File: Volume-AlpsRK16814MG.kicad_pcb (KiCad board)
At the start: 2 copper layers, 62.2 x 32.4 mm, 7 parts, among them P1 AB I/O, P2 CD I/O, P3 VD, P4 CTRL, U1 SN754410

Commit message: Routed.
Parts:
- moved C1 0.51 mm to (121.2, 110.5)
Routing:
- net +5VD: track 0.00 -> 57.6 mm
- net GND: track 16.5 -> 68.7 mm, vias 0 -> 4
- net DGND: track 7.89 -> 52.4 mm
- net /VOL_UP: track 0.00 -> 31.3 mm
- net /C_TOP: track 0.00 -> 29.9 mm
- net /A_TOP: track 0.00 -> 25.8 mm
- net /D_TOP: track 0.00 -> 24.9 mm
- net /CD_COMMON: track 0.00 -> 24.7 mm
- net /B_TOP: track 0.00 -> 22.9 mm
- net /B_WIPER: track 0.00 -> 22.3 mm
- net /D_WIPER: track 0.00 -> 20.2 mm
- net /AB_COMMON: track 0.00 -> 17.5 mm
- net /C_WIPER: track 0.00 -> 15.9 mm
- net /A_WIPER: track 0.00 -> 12.1 mm
- net /VOL_DOWN: track 0.00 -> 11.7 mm
- added copper zone on B.Cu, net DGND
- added copper zone on F.Cu, net DGND
- added copper zone on F.Cu, net GND
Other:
- board size 62.2 x 32.4 mm -> 62.9 x 32.4 mm

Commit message: Flooded.
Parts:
- added P5: GND, mfk-AVA-20ga, F.Cu at (144.1, 116.2)
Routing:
- net GND: track 68.7 -> 95.9 mm, vias 4 -> 7
- added copper zone on B.Cu, net GND

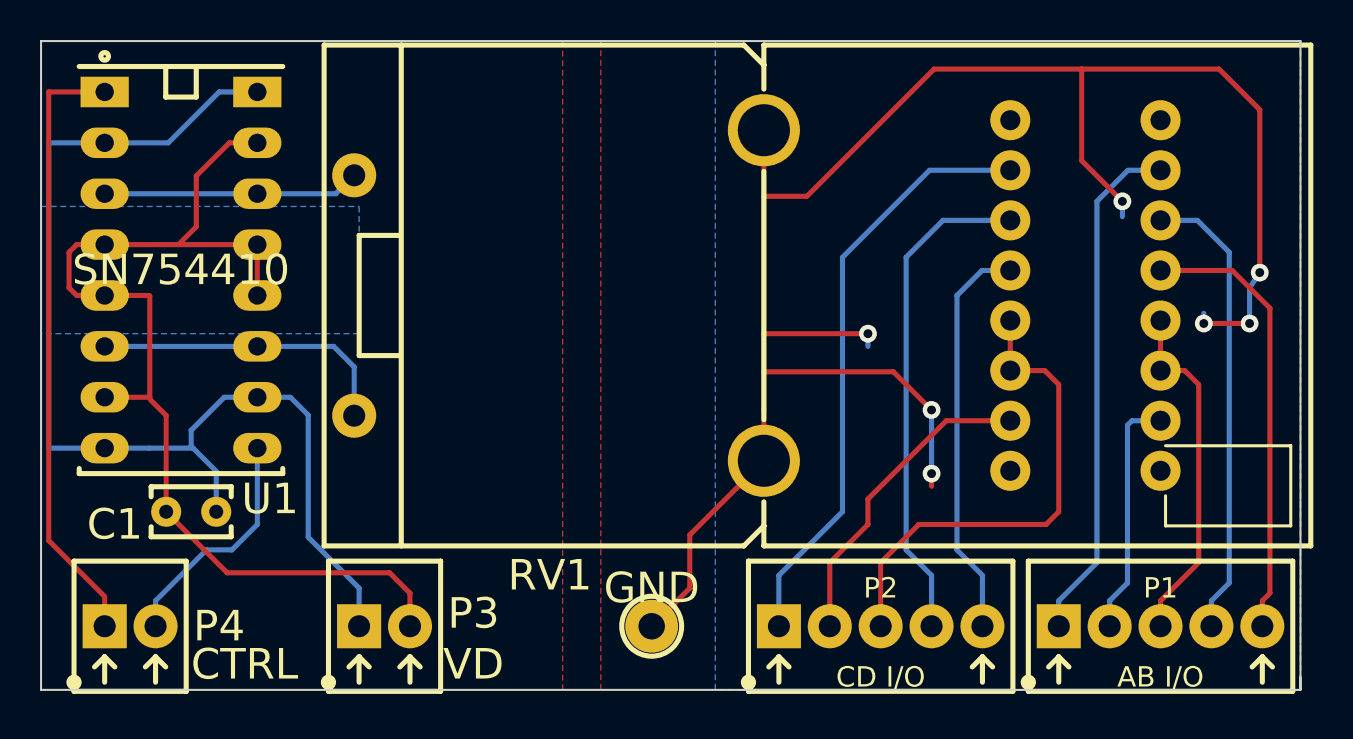
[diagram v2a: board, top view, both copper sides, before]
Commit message: Added bypass C to VCC2.
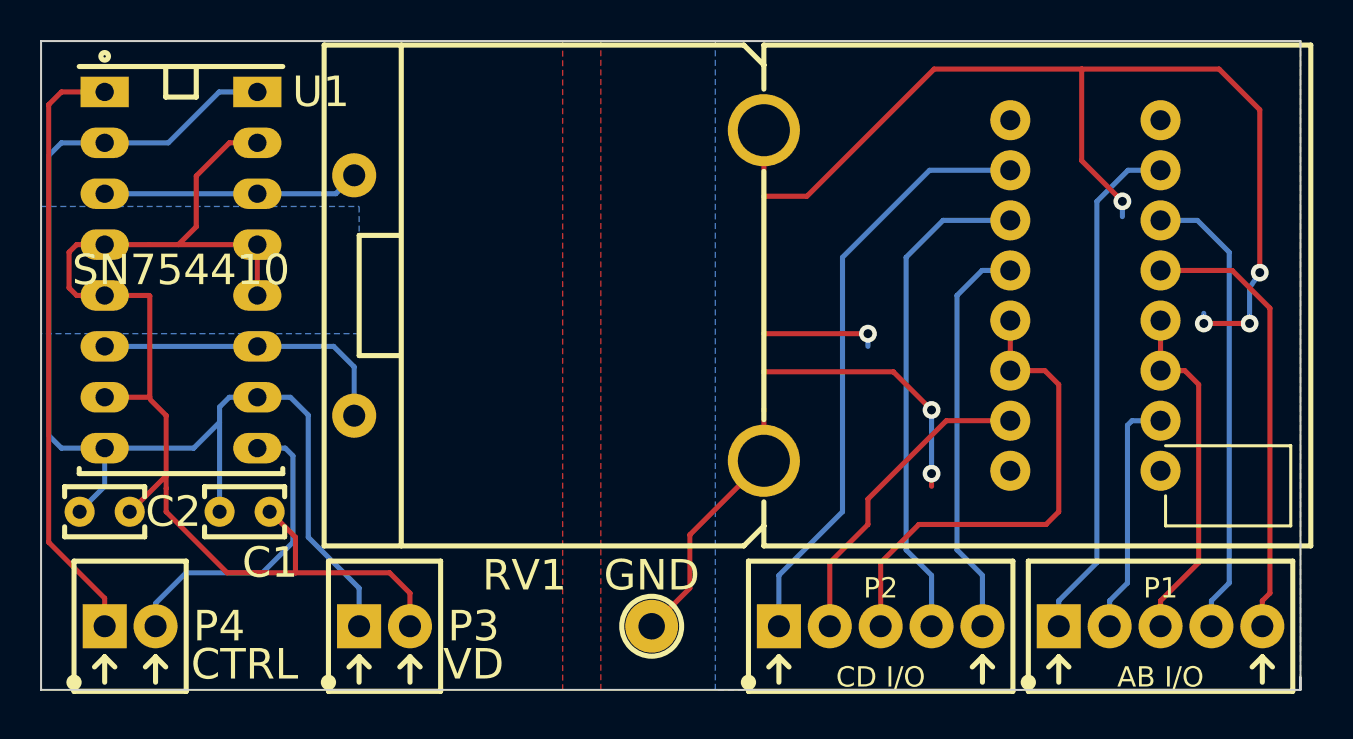
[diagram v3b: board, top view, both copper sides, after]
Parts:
- added C2: 1u, mfk-C_4.0_2.5_2.5_0.5, F.Cu at (116.8, 110.5)
- moved C1 2.67 mm to (123.8, 110.5), turned to 0 degrees
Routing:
- net DGND: track 52.4 -> 58.6 mm
- net /VOL_DOWN: track 11.7 -> 15.5 mm
- net +5VD: track 57.6 -> 60.5 mm
- net /VOL_UP: track 31.3 -> 30.2 mm

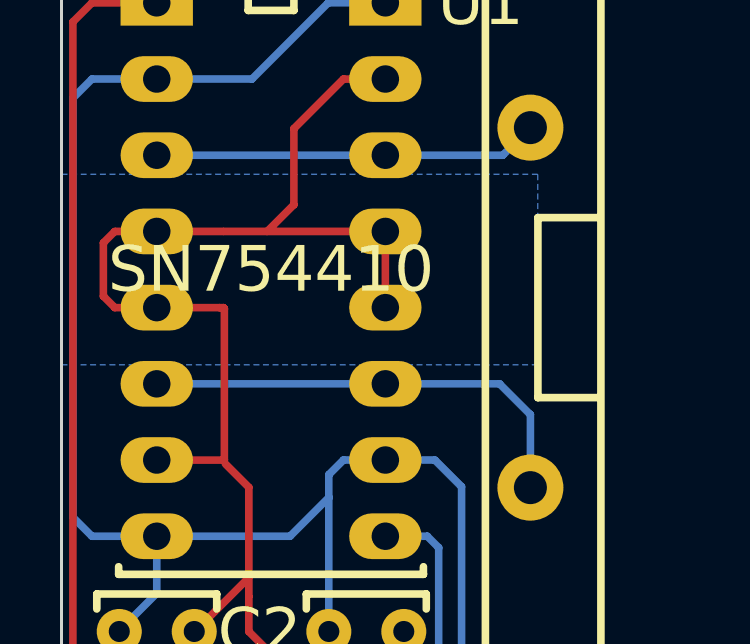
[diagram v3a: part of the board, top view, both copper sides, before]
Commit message: Added cap to VCC2. Stitched SN754410 GND for heat.
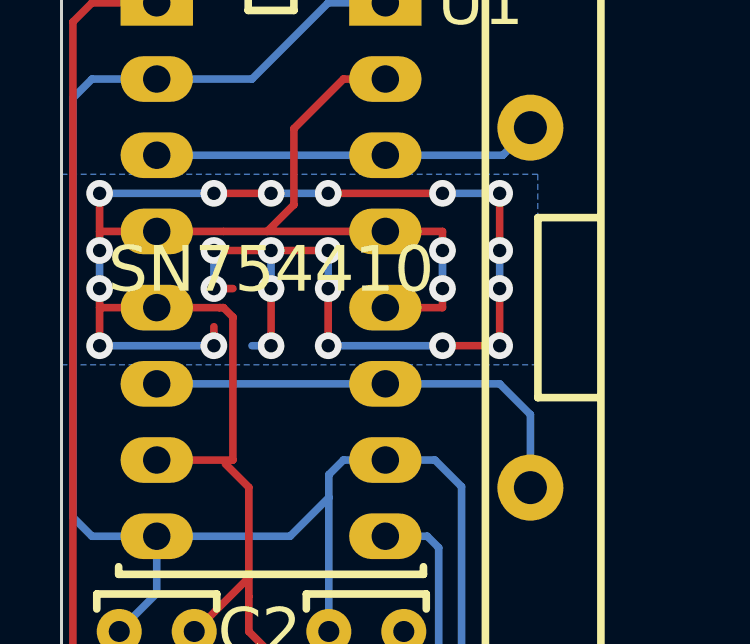
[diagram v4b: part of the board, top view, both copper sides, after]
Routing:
- net DGND: track 58.6 -> 107.3 mm, vias 0 -> 24
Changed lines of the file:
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@@
     (links 34)
     (no_connects 0)
-    (area 113.614999 86.944999 176.580001 119.430001)
+    (area 113.292467 86.559999 187.375714 124.62)
     (thickness 1.6)
     (drawings 7)
-    (tracks 162)
+    (tracks 213)
     (zones 0)
     (modules 9)
@@
   (segment (start 114.046 112.014) (end 114.046 90.17) (width 0.254) (layer F.Cu) (net 13))
   (segment (start 116.84 114.808) (end 114.046 112.014) (width 0.254) (layer F.Cu) (net 13))
+  (segment (start 120.65 97.79) (end 118.745 97.79) (width 0.254) (layer F.Cu) (net 14))
+  (segment (start 118.745 99.06) (end 119.38 99.06) (width 0.254) (layer F.Cu) (net 14))
+  (via (at 118.745 99.06) (size 0.889) (layers F.Cu B.Cu) (net 14))
+  (segment (start 118.745 97.79) (end 118.745 99.06) (width 0.254) (layer B.Cu) (net 14))
+  (via (at 118.745 97.79) (size 0.889) (layers F.Cu B.Cu) (net 14))
+  (segment (start 128.27 100.965) (end 126.365 100.965) (width 0.254) (layer F.Cu) (net 14))
+  (via (at 118.745 95.885) (size 0.889) (layers F.Cu B.Cu) (net 14))
+  (segment (start 118.745 95.885) (end 120.65 95.885) (width 0.254) (layer F.Cu) (net 14))
+  (via (at 120.65 95.885) (size 0.889) (layers F.Cu B.Cu) (net 14))
+  (segment (start 120.65 95.885) (end 122.555 95.885) (width 0.254) (layer B.Cu) (net 14))
+  (via (at 122.555 95.885) (size 0.889) (layers F.Cu B.Cu) (net 14))
+  (segment (start 122.555 95.885) (end 126.365 95.885) (width 0.254) (layer F.Cu) (net 14))
+  (via (at 126.365 95.885) (size 0.889) (layers F.Cu B.Cu) (net 14))
+  (segment (start 126.365 95.885) (end 128.27 95.885) (width 0.254) (layer B.Cu) (net 14))
+  (via (at 128.27 95.885) (size 0.889) (layers F.Cu B.Cu) (net 14))
+  (segment (start 128.27 95.885) (end 128.27 97.79) (width 0.254) (layer F.Cu) (net 14))
+  (via (at 128.27 97.79) (size 0.889) (layers F.Cu B.Cu) (net 14))
+  (segment (start 128.27 97.79) (end 128.27 99.06) (width 0.254) (layer B.Cu) (net 14))
+  (via (at 128.27 99.06) (size 0.889) (layers F.Cu B.Cu) (net 14))
+  (segment (start 128.27 99.06) (end 128.27 100.965) (width 0.254) (layer F.Cu) (net 14))
+  (via (at 128.27 100.965) (size 0.889) (layers F.Cu B.Cu) (net 14))
+  (segment (start 114.935 97.155) (end 114.935 95.885) (width 0.254) (layer F.Cu) (net 14))
+  (via (at 114.935 95.885) (size 0.889) (layers F.Cu B.Cu) (net 14))
+  (segment (start 114.935 95.885) (end 118.745 95.885) (width 0.254) (layer B.Cu) (net 14))
+  (segment (start 120.65 100.965) (end 120.015 100.965) (width 0.254) (layer B.Cu) (net 14))
+  (via (at 120.65 100.965) (size 0.889) (layers F.Cu B.Cu) (net 14))
+  (segment (start 120.65 99.06) (end 120.65 100.965) (width 0.254) (layer F.Cu) (net 14))
+  (via (at 120.65 99.06) (size 0.889) (layers F.Cu B.Cu) (net 14))
+  (segment (start 120.65 97.79) (end 120.65 99.06) (width 0.254) (layer B.Cu) (net 14))
+  (via (at 120.65 97.79) (size 0.889) (layers F.Cu B.Cu) (net 14))
+  (segment (start 122.555 97.79) (end 120.65 97.79) (width 0.254) (layer F.Cu) (net 14))
+  (via (at 122.555 97.79) (size 0.889) (layers F.Cu B.Cu) (net 14))
+  (segment (start 122.555 99.06) (end 122.555 97.79) (width 0.254) (layer B.Cu) (net 14))
+  (via (at 122.555 99.06) (size 0.889) (layers F.Cu B.Cu) (net 14))
+  (segment (start 122.555 100.965) (end 122.555 99.06) (width 0.254) (layer F.Cu) (net 14))
+  (via (at 122.555 100.965) (size 0.889) (layers F.Cu B.Cu) (net 14))
+  (segment (start 126.365 100.965) (end 122.555 100.965) (width 0.254) (layer B.Cu) (net 14))
+  (via (at 126.365 100.965) (size 0.889) (layers F.Cu B.Cu) (net 14))
+  (segment (start 118.745 100.33) (end 118.745 100.965) (width 0.254) (layer F.Cu) (net 14))
+  (via (at 118.745 100.965) (size 0.889) (layers F.Cu B.Cu) (net 14))
+  (segment (start 114.935 100.965) (end 114.935 99.695) (width 0.254) (layer F.Cu) (net 14))
+  (via (at 114.935 100.965) (size 0.889) (layers F.Cu B.Cu) (net 14))
+  (segment (start 114.935 100.965) (end 118.745 100.965) (width 0.254) (layer B.Cu) (net 14))
+  (segment (start 124.46 97.155) (end 126.365 97.155) (width 0.254) (layer F.Cu) (net 14))
+  (segment (start 126.365 99.695) (end 124.46 99.695) (width 0.254) (layer F.Cu) (net 14))
+  (segment (start 126.365 99.06) (end 126.365 99.695) (width 0.254) (layer F.Cu) (net 14))
+  (via (at 126.365 99.06) (size 0.889) (layers F.Cu B.Cu) (net 14))
+  (segment (start 126.365 97.79) (end 126.365 99.06) (width 0.254) (layer B.Cu) (net 14))
+  (via (at 126.365 97.79) (size 0.889) (layers F.Cu B.Cu) (net 14))
+  (segment (start 126.365 97.155) (end 126.365 97.79) (width 0.254) (layer F.Cu) (net 14))
+  (segment (start 116.84 97.155) (end 114.935 97.155) (width 0.254) (layer F.Cu) (net 14))
+  (segment (start 114.935 99.695) (end 116.84 99.695) (width 0.254) (layer F.Cu) (net 14))
+  (segment (start 114.935 99.06) (end 114.935 99.695) (width 0.254) (layer F.Cu) (net 14))
+  (via (at 114.935 99.06) (size 0.889) (layers F.Cu B.Cu) (net 14))
+  (segment (start 114.935 97.79) (end 114.935 99.06) (width 0.254) (layer B.Cu) (net 14))
+  (via (at 114.935 97.79) (size 0.889) (layers F.Cu B.Cu) (net 14))
+  (segment (start 114.935 97.155) (end 114.935 97.79) (width 0.254) (layer F.Cu) (net 14))
   (segment (start 118.08968 110.49) (end 118.11 110.49) (width 0.254) (layer F.Cu) (net 14))
   (segment (start 118.11 110.49) (end 119.90832 108.69168) (width 0.254) (layer F.Cu) (net 14))
@@
   (segment (start 126.365 113.538) (end 122.95632 113.538) (width 0.254) (layer F.Cu) (net 14))
   (segment (start 132.08 114.554) (end 131.064 113.538) (width 0.254) (layer F.Cu) (net 14))
-  (segment (start 116.84 99.695) (end 115.443 99.695) (width 0.254) (layer F.Cu) (net 14))
-  (segment (start 115.443 97.155) (end 116.84 97.155) (width 0.254) (layer F.Cu) (net 14))
-  (segment (start 115.062 97.536) (end 115.443 97.155) (width 0.254) (layer F.Cu) (net 14))
-  (segment (start 115.062 99.314) (end 115.062 97.536) (width 0.254) (layer F.Cu) (net 14))
-  (segment (start 115.443 99.695) (end 115.062 99.314) (width 0.254) (layer F.Cu) (net 14))
   (segment (start 124.46 92.075) (end 123.063 92.075) (width 0.254) (layer F.Cu) (net 14))
   (segment (start 121.412 96.266) (end 120.523 97.155) (width 0.254) (layer F.Cu) (net 14))
@@
   (segment (start 119.0628 97.155) (end 120.523 97.155) (width 0.254) (layer F.Cu) (net 14))
   (segment (start 120.523 97.155) (end 124.46 97.155) (width 0.254) (layer F.Cu) (net 14))
-  (segment (start 124.46 97.155) (end 124.46 99.695) (width 0.254) (layer F.Cu) (net 14))
   (segment (start 132.08 116.205) (end 132.08 114.554) (width 0.254) (layer F.Cu) (net 14))
   (segment (start 117.475 97.155) (end 119.0628 97.155) (width 0.254) (layer F.Cu) (net 14))
-  (segment (start 117.475 104.775) (end 119.0943 104.775) (width 0.254) (layer F.Cu) (net 14))
-  (segment (start 119.0943 99.7265) (end 119.0628 99.695) (width 0.254) (layer F.Cu) (net 14))
-  (segment (start 119.0943 104.775) (end 119.0943 99.7265) (width 0.254) (layer F.Cu) (net 14))
+  (segment (start 117.475 104.775) (end 119.38 104.775) (width 0.254) (layer F.Cu) (net 14))
+  (segment (start 119.38 100.0122) (end 119.0628 99.695) (width 0.254) (layer F.Cu) (net 14))
+  (segment (start 119.38 104.775) (end 119.38 100.0122) (width 0.254) (layer F.Cu) (net 14))
   (segment (start 117.475 99.695) (end 118.9357 99.695) (width 0.254) (layer F.Cu) (net 14))
   (segment (start 118.9357 99.695) (end 119.0628 99.695) (width 0.254) (layer F.Cu) (net 14))

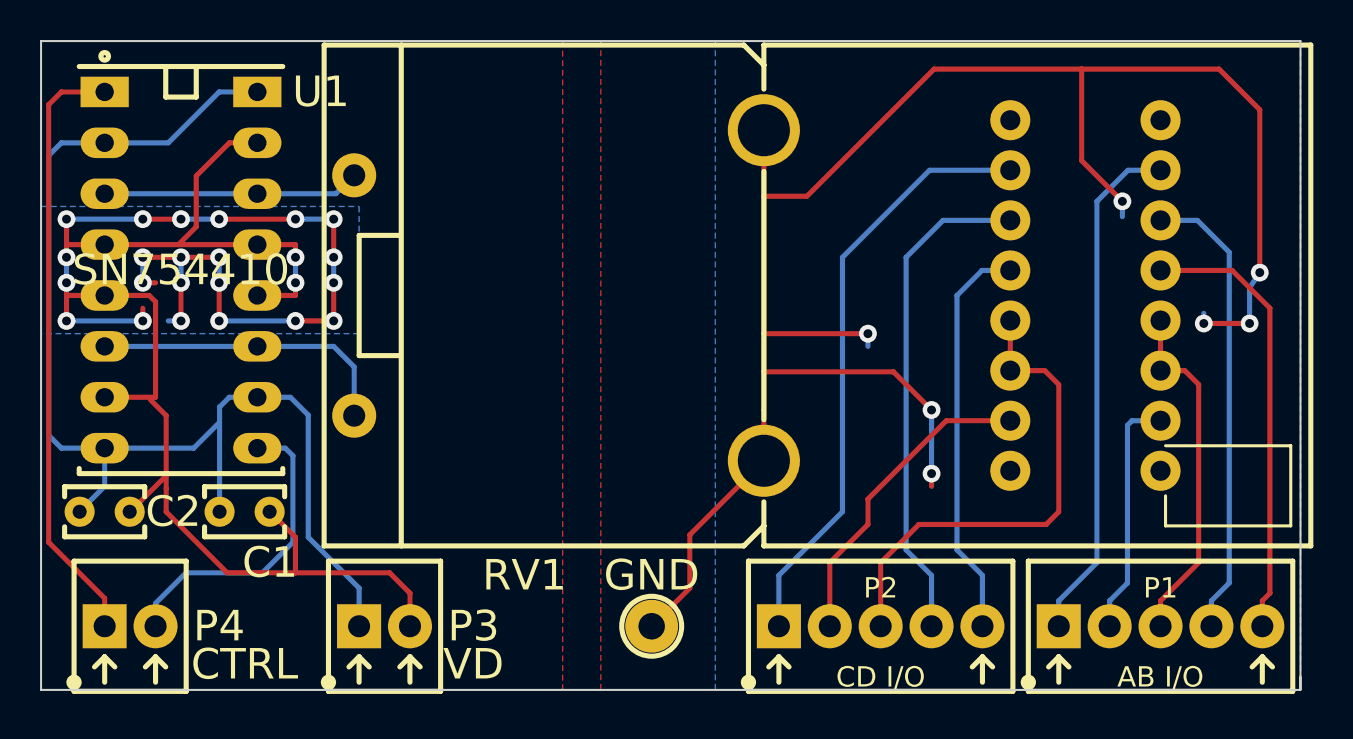
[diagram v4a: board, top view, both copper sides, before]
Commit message: Added (C) and other additional labels silkscreen.
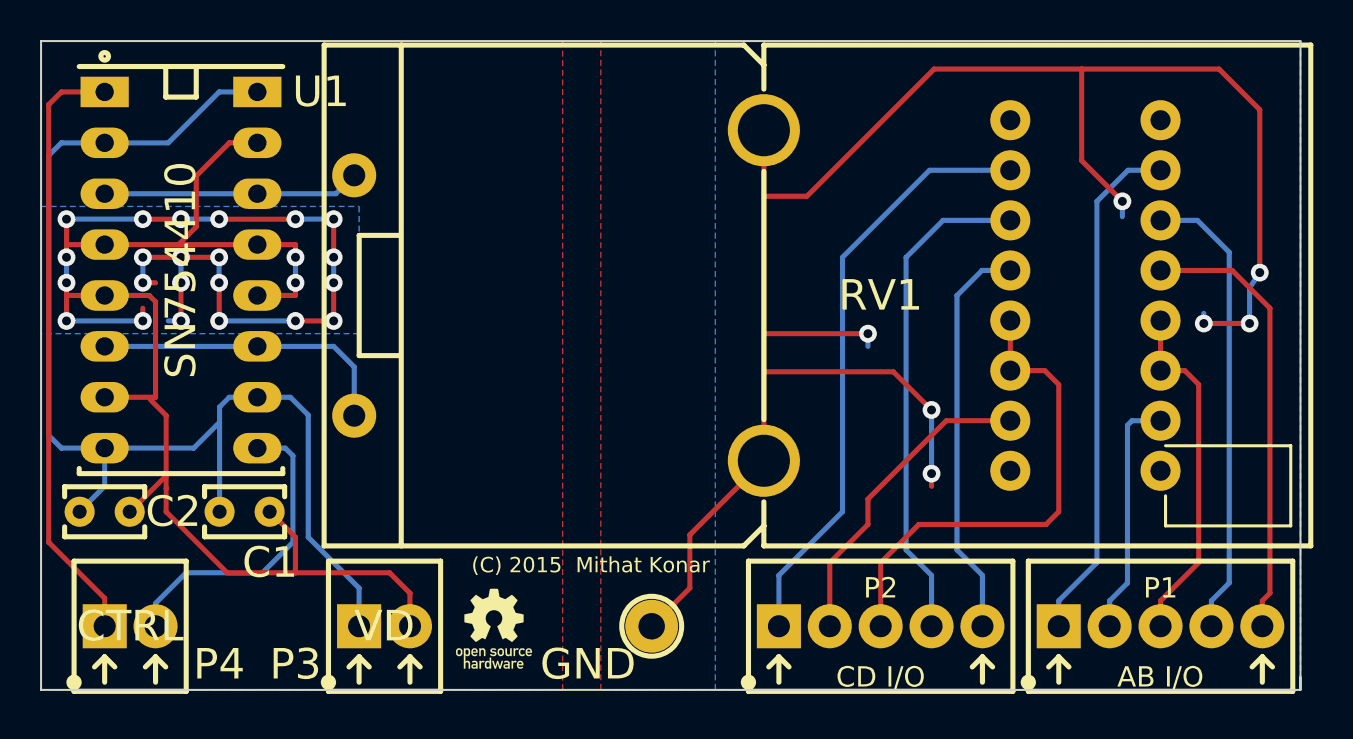
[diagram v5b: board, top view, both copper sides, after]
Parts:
- added VAL: REF, oshw-logo-150mil-FSilk, F.Cu at (136.3, 116.3)
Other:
- board text added: "(C) 2015 Mithat Konar"
- board text added: "+5VDC"
- board text added: "AB_COMMON"
- board text added: "A_TOP"
- board text added: "A_WIPER"
- board text added: "B_TOP"
- board text added: "B_WIPER"
- board text added: "CD_COMMON"
- board text added: "CHASSIS GND"
- board text added: "C_TOP"
- board text added: "C_WIPER"
- board text added: "DGND"
- board text added: "D_TOP"
- board text added: "D_WIPER"
- board text added: "VOL_DOWN"
- board text added: "VOL_UP"

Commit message: Silkscreen optimizations. Added license to silkscreen.
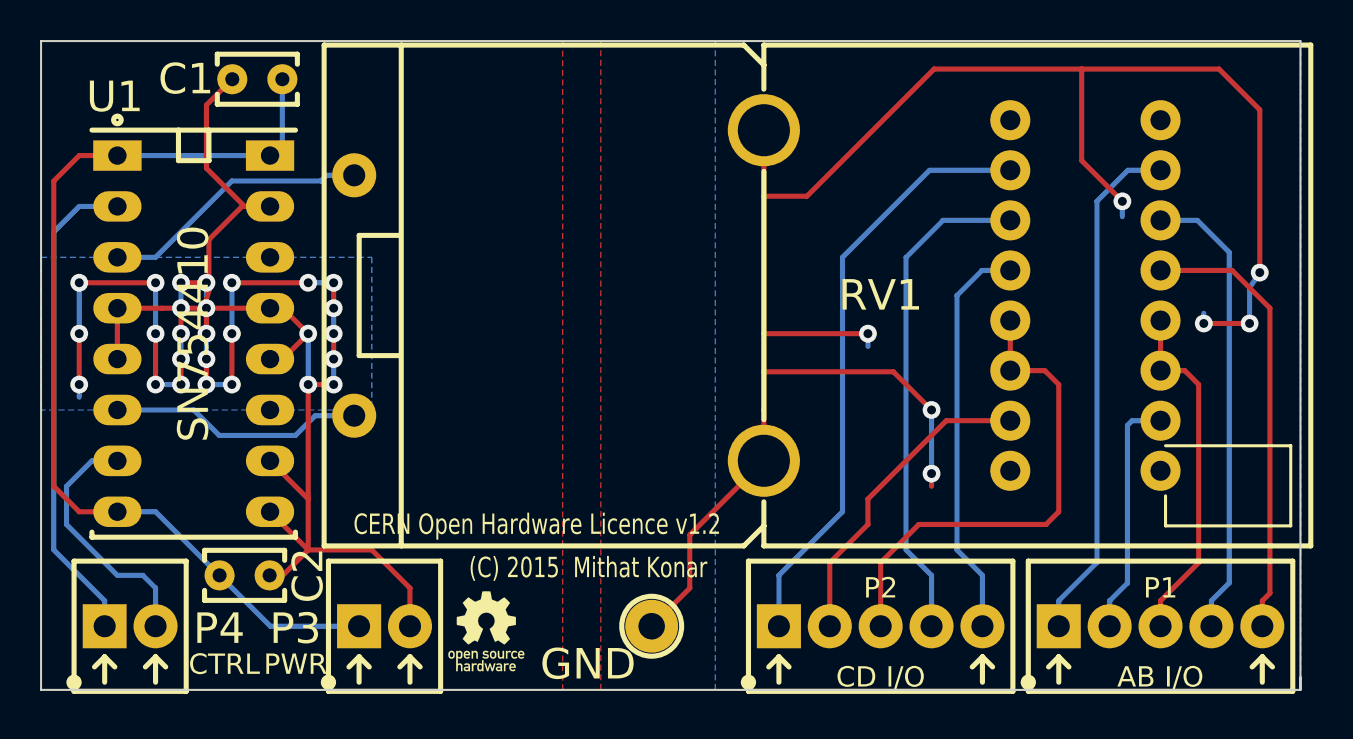
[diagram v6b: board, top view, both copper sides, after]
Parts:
- P3: value VD -> PWR
- moved C1 21.6 mm to (124.5, 88.9), turned to 180 degrees
- moved C2 7.67 mm to (123.8, 113.7)
- moved U1 3.24 mm to (121.3, 101.6)
- moved VAL 0.40 mm to (135.9, 116.5)
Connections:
- RV1 pad 19: N-0000016 -> N-000004
- RV1 pad 20: N-0000018 -> N-0000020
- U1 pad 1: /VOL_UP -> +5VD
- U1 pad 10: +5VD -> DGND
- U1 pad 11: N-0000018 -> (no net)
- U1 pad 14: N-0000016 -> (no net)
- U1 pad 2: +5VD -> /VOL_UP
- U1 pad 3: N-0000016 -> N-000004
- U1 pad 6: N-0000018 -> N-0000020
- U1 pad 7: DGND -> /VOL_DOWN
- U1 pad 9: /VOL_DOWN -> DGND
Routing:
- net N-0000018: track 15.3 -> 0.00 mm
- net N-000004: track 0.00 -> 13.5 mm
- net N-0000016: track 12.8 -> 0.00 mm
- net N-0000020: track 0.00 -> 12.8 mm
- net +5VD: track 60.5 -> 48.8 mm
- net DGND: track 107.3 -> 100.1 mm, vias 24 -> 27
- net /VOL_UP: track 30.2 -> 24.4 mm
- net /VOL_DOWN: track 15.5 -> 12.6 mm
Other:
- board text added: "CERN Open Hardware Licence v1.2"

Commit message: Silk tweaks.
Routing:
- net DGND: track 100.1 -> 102.0 mm
